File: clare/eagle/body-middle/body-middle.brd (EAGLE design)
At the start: 36 x 55 mm, 10 parts

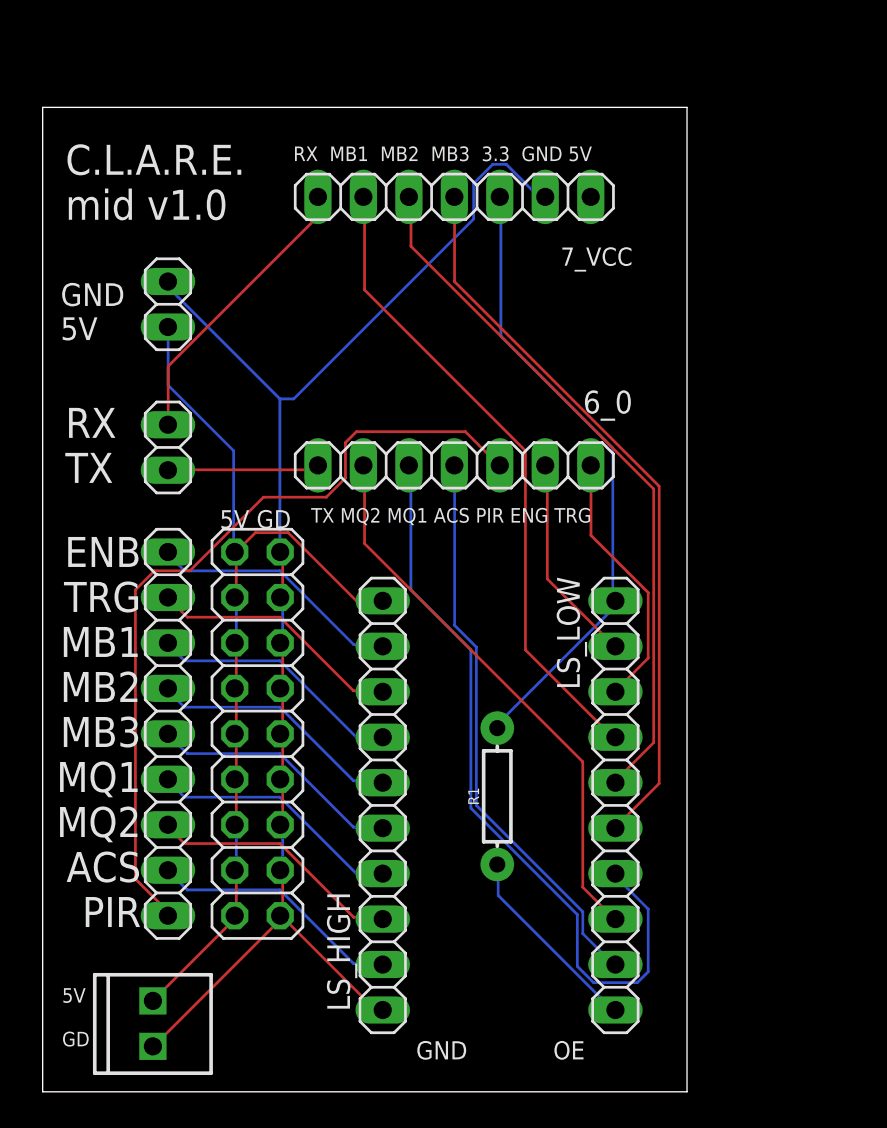
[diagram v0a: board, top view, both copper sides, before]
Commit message: New arduino nano pcb for body middle with working code
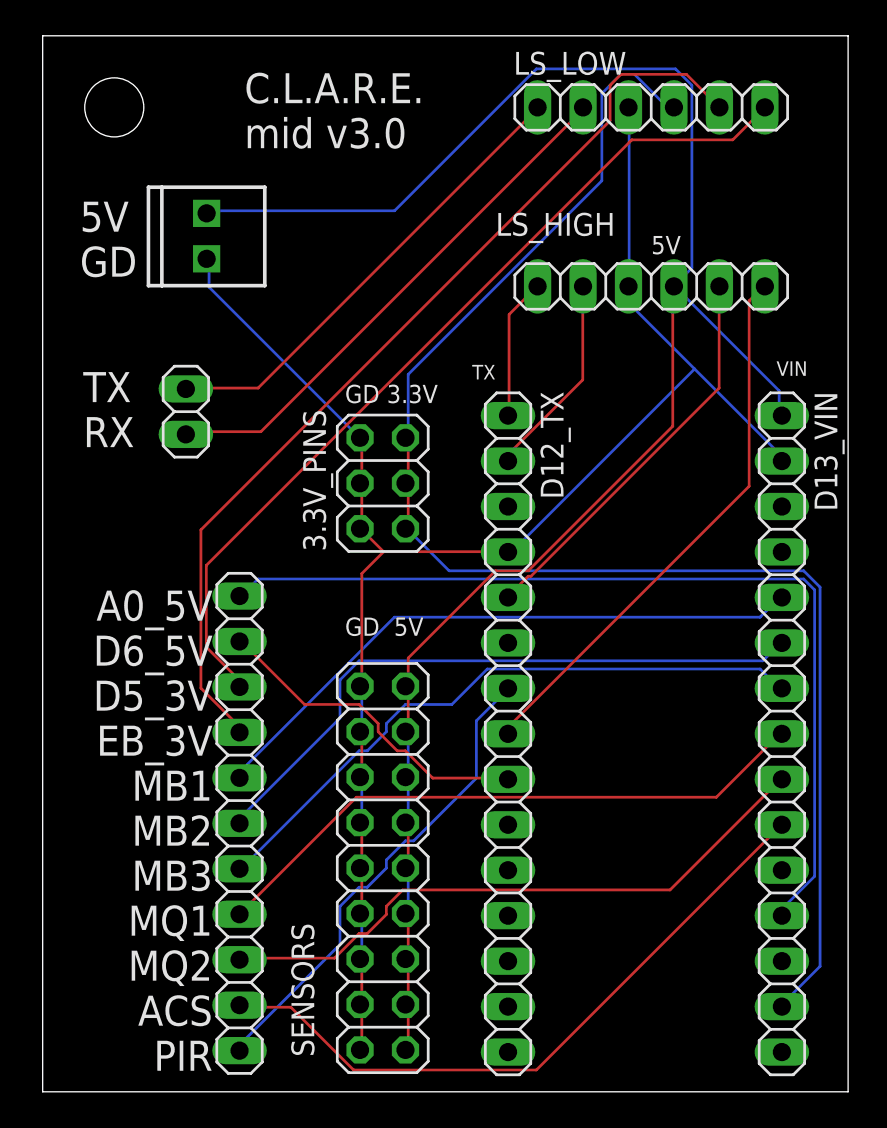
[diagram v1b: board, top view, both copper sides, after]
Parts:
- removed 6_0, 7_VCC: (no value), pinhead:1X07
- removed INPUTS: (no value), pinhead:1X09
- removed JP1: (no value), pinhead:2X09
- removed R1: 10k, SparkFun-Resistors:AXIAL-0.3
- removed XIAO_PWR: (no value), pinhead:1X02
- added 3.3V_PINS: (no value), pinhead:2X03
- added 5V_PINS: (no value), pinhead:2X09
- added D12_TX, D13_VIN: (no value), pinhead:1X15
- added SENSORS: (no value), pinhead:1X11
- LS_HIGH, LS_LOW: device pinhead:1X10 -> pinhead:1X06
- moved POWER 44.1 mm to (9.16, 46.5)
- moved LS_LOW 39.1 mm to (34.0, 55.0), turned to 0 degrees
- moved LS_HIGH 32.6 mm to (34.0, 45.0), turned to 0 degrees
- moved SERIAL 2.24 mm to (8.00, 38.0), turned to 90 degrees
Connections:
- removed net ENB: INPUTS.9, LS_HIGH.9
- removed net OE: LS_LOW.10, R1.P$1
- removed net TRG: INPUTS.8, LS_HIGH.8
- removed net VCC: 7_VCC.1
- removed net XACS: 6_0.4, LS_LOW.9
- removed net XENB: 6_0.2, LS_LOW.2
- removed net XMB1: 7_VCC.6, LS_LOW.4
- removed net XMB2: 7_VCC.5, LS_LOW.5
- removed net XMB3: 7_VCC.4, LS_LOW.6
- removed net XMQ1: 6_0.5, LS_LOW.7
- removed net XMQ2: 6_0.6, LS_LOW.8
- removed net XTRG: 6_0.1, LS_LOW.3
- new net A05V: D13_VIN.12, SENSORS.11
- new net D53.3: LS_LOW.6, SENSORS.9
- new net D55V: D12_TX.8, LS_HIGH.6
- new net D65V: D12_TX.9, SENSORS.10
- new net ENB3.3: LS_LOW.5, SENSORS.8
- new net ENB5V: D12_TX.5, LS_HIGH.5
- new net RX5V: D12_TX.2, LS_HIGH.2
- new net TRG5V: D12_TX.6
- new net TX5V: D12_TX.1, LS_HIGH.1
- net 3.3V: now also 3.3V_PINS.1, 3.3V_PINS.3, 3.3V_PINS.5, D13_VIN.14, LS_LOW.4; no longer 7_VCC.3, LS_LOW.1, R1.P$2
- net 5V: now also 5V_PINS.1, 5V_PINS.11, 5V_PINS.13, 5V_PINS.15, 5V_PINS.17, 5V_PINS.3, 5V_PINS.5, 5V_PINS.7, 5V_PINS.9, D13_VIN.1, LS_HIGH.4; no longer JP1.1, JP1.11, JP1.13, JP1.15, JP1.17, JP1.3, JP1.5, JP1.7, JP1.9, LS_HIGH.10, XIAO_PWR.2
- net ACS: now also D13_VIN.10, SENSORS.2; no longer INPUTS.2, LS_HIGH.2
- net GND: now also 3.3V_PINS.2, 3.3V_PINS.4, 3.3V_PINS.6, 5V_PINS.10, 5V_PINS.12, 5V_PINS.14, 5V_PINS.16, 5V_PINS.18, 5V_PINS.2, 5V_PINS.4, 5V_PINS.6, 5V_PINS.8, D12_TX.4, D13_VIN.2, LS_HIGH.3, LS_LOW.3; no longer 7_VCC.2, JP1.10, JP1.12, JP1.14, JP1.16, JP1.18, JP1.2, JP1.4, JP1.6, JP1.8, LS_HIGH.1, XIAO_PWR.1
- net MB1: now also D13_VIN.5, SENSORS.7; no longer INPUTS.7, LS_HIGH.7
- net MB2: now also D13_VIN.6, SENSORS.6; no longer INPUTS.6, LS_HIGH.6
- net MB3: now also D13_VIN.7, SENSORS.5; no longer INPUTS.5, LS_HIGH.5
- net MQ1: now also D13_VIN.8, SENSORS.4; no longer INPUTS.4, LS_HIGH.4
- net MQ2: now also D13_VIN.9, SENSORS.3; no longer INPUTS.3, LS_HIGH.3
- net PIR: now also D12_TX.7, SENSORS.1; no longer 6_0.3, INPUTS.1
- net RX: now also LS_LOW.2; no longer 7_VCC.7
- net TX: now also LS_LOW.1; no longer 6_0.7
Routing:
- net ENB3.3: track 0.00 -> 53.6 mm
- net A05V: track 0.00 -> 51.7 mm
- net 5V: track 52.2 -> 103.8 mm
- net D53.3: track 0.00 -> 49.4 mm
- net 3.3V: track 35.3 -> 83.3 mm
- net XMQ1: track 42.7 -> 0.00 mm
- net XMB3: track 41.0 -> 0.00 mm
- net XMB2: track 39.3 -> 0.00 mm
- net XMB1: track 36.1 -> 0.00 mm
- net XACS: track 31.7 -> 0.00 mm
- net XMQ2: track 31.2 -> 0.00 mm
- net D55V: track 0.00 -> 31.0 mm
- net ACS: track 14.2 -> 37.5 mm
- net ENB5V: track 0.00 -> 22.3 mm
- net MB2: track 14.3 -> 35.9 mm
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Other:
- board size 36 x 55 mm -> 45 x 59 mm
- board text added: "5V"
- board text added: "A0_5V D6_5V D5_3V EB_3V MB1 MB2 MB3 MQ1 MQ2 ACS PIR"
- board text added: "C.L.A.R.E. mid v3.0"
- board text added: "GD 3.3V"
- board text added: "GD 5V"
- board text added: "TX"
- board text added: "TX RX"
- board text added: "VIN"
- board text removed: "C.L.A.R.E. mid v1.0"
- board text removed: "ENB TRG MB1 MB2 MB3 MQ1 MQ2 ACS PIR"
- board text removed: "GND 5V"
- board text removed: "GND OE"
- board text removed: "RX MB1 MB2 MB3 3.3 GND 5V"
- board text removed: "RX TX"
- board text removed: "TX MQ2 MQ1 ACS PIR ENG TRG"
